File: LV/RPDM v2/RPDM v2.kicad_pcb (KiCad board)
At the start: 2 copper layers, 127.5 x 99.9 mm, 106 parts, among them J2 1-770669-1, J3 776180-1, U1 i7A24045A033V-001-R, U5 OKI-78SR-5_1.5-W36-C

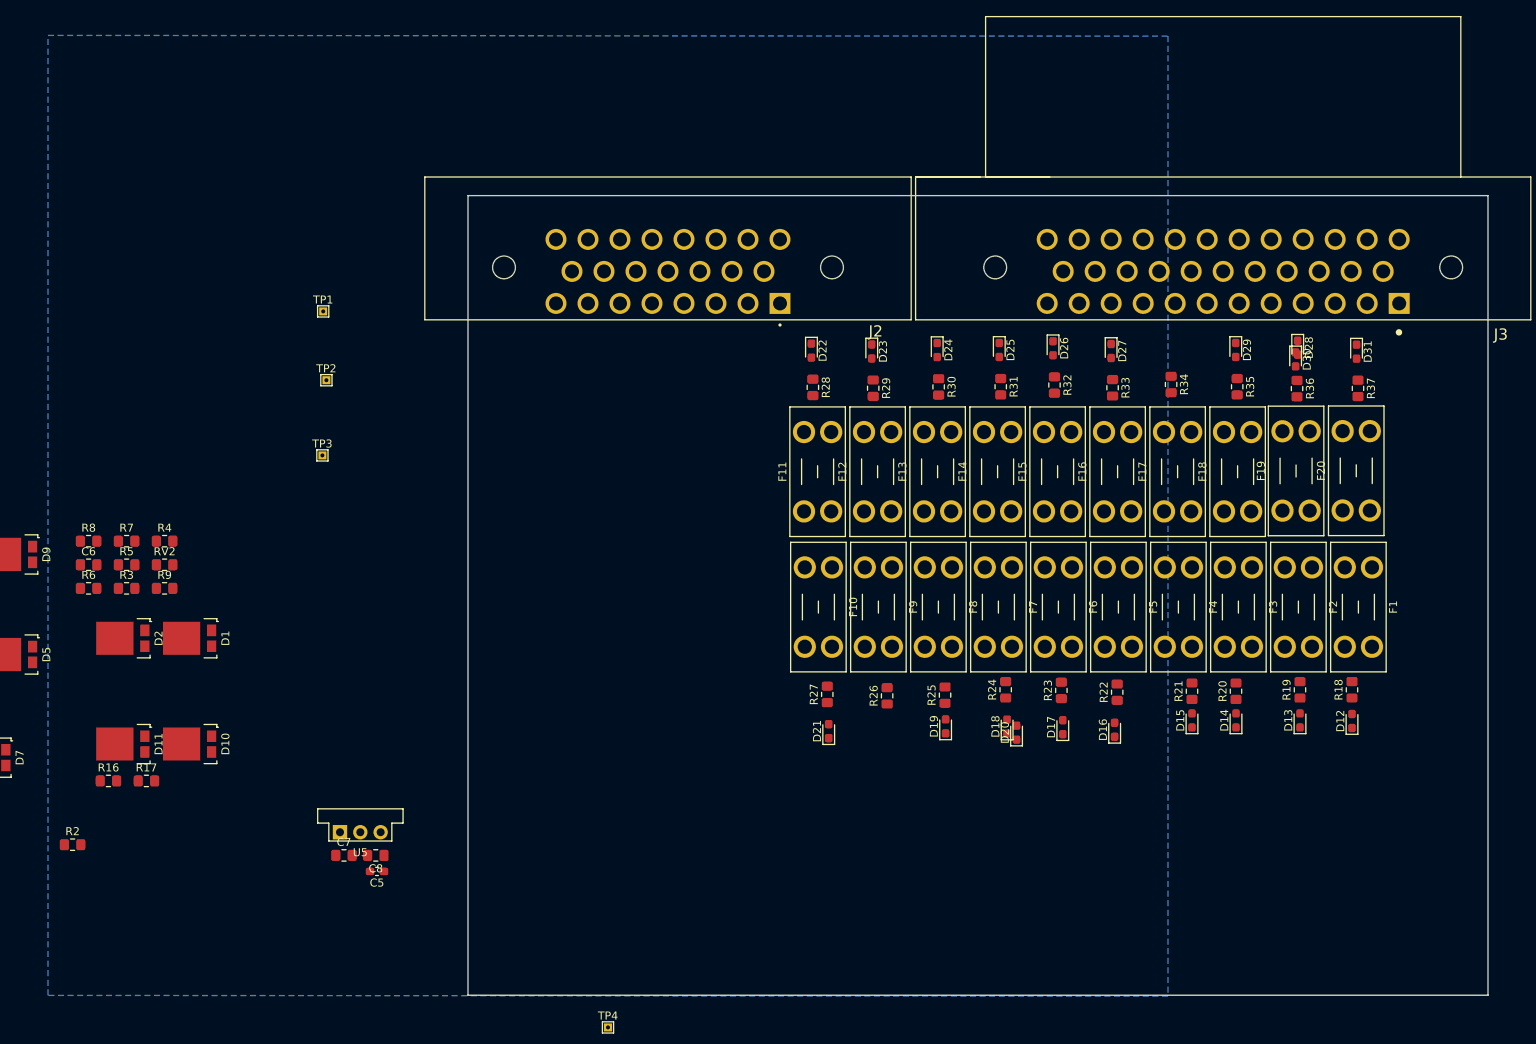
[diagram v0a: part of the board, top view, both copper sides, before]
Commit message: rpdm, libraries cleanup
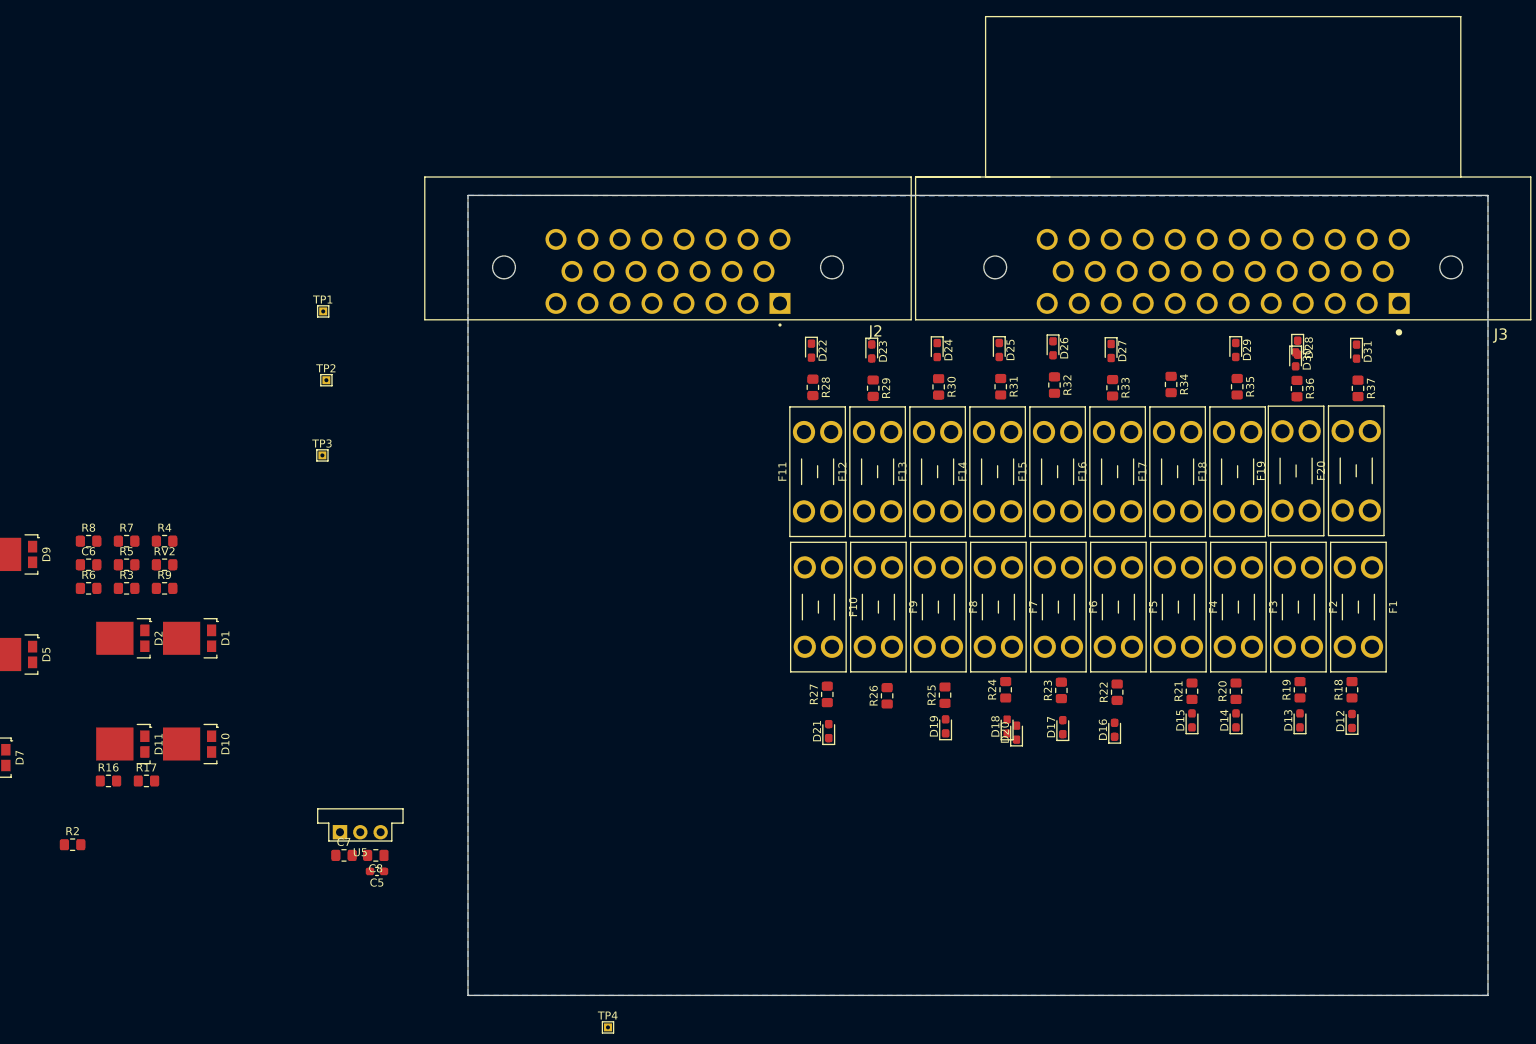
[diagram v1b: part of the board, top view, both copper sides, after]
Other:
- board size 127.5 x 99.9 mm -> 127.5 x 100 mm
- copper layers 2 -> 4
- net class Default: clearance 0.2 -> 0.127; trace_width 0.25 -> 0.127; via_dia 0.8 -> 0.6; via_drill 0.4 -> 0.3
- rule trace_clearance: 0.2 -> 0.127
- rule trace_min: 0.2 -> 0.127
- rule via_min_size: 0.4 -> 0.6

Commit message: RPDM
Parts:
- removed D27, D28, D31: OK_LED, Diode_SMD:D_0603_1608Metric_Pad1.05x0.95mm_HandSolder
- removed F19, F20: Fuse, Fuse:Fuseholder_Blade_Mini_Keystone_3568
- removed R34, R35: 10k, Resistor_SMD:R_0805_2012Metric_Pad1.15x1.40mm_HandSolder
- removed U1: i7A24045A033V-001-R, DCDC:i7A24045A033V
- added C10: 330uF, Capacitor_THT:CP_Radial_D10.0mm_P5.00mm, F.Cu at (303.3, 213.1)
- added C9: 22µF, UOWM_Capacitors:C_Murata_KCM55, F.Cu at (293.7, 212.3)
- added J1: 24V_IN, UOWM_TerminalBlocks:EB167A-03-M, F.Cu at (195.3, 201.1)
- added K1: G8NW, UOWM_Relays:Omron-G8NW-2L-AS_SK-MFG, F.Cu at (301.4, 181.4)
- added K2: G8NW, UOWM_Relays:Omron-G8NW-2L-AS_SK-MFG, F.Cu at (317.7, 181.4)
- added K3: J115F, UOWM_Relays:CIT_J115F1, F.Cu at (237.9, 208.2)
- added Q1: Q_Dual_PMOS, Package_SO:TSOP-6_1.65x3.05mm_P0.95mm, F.Cu at (175.8, 186.3)
- added Q2: Q_Dual_NMOS, UOWM_Package_SO:Diodes_SO-8_5.3x6.2mm_P1.27mm, B.Cu at (309.7, 248.4)
- added Q3: Q_Dual_NMOS, UOWM_Package_SO:Diodes_SO-8_5.3x6.2mm_P1.27mm, F.Cu at (333.4, 250.0)
- added R38: 10k, Resistor_SMD:R_0805_2012Metric_Pad1.15x1.40mm_HandSolder, B.Cu at (160.8, 188.2)
- added U3: OKI-78SR-5_1.5-W36-C, Converter_DCDC:Converter_DCDC_muRata_OKI-78SR_Vertical, F.Cu at (321.0, 213.5)
- added U4: ACS71240, UOWM_Sensors:Allegro_MicroSystems_LLC-LCB-8-0-0-IPC_A, F.Cu at (246.8, 195.2)
- C1: value 330µF -> 0.1µF; footprint Capacitor_THT:CP_Radial_D10.0mm_P5.00mm -> Capacitor_SMD:C_0603_1608Metric_Pad1.05x0.95mm_HandSolder
- C2: value 22µF -> 1uF; footprint Capacitor_extra:C_Murata_KCM55 -> Capacitor_SMD:C_0805_2012Metric_Pad1.15x1.40mm_HandSolder; moved to B.Cu
- C3: value 22µF -> 0.1µF; footprint Capacitor_extra:C_Murata_KCM55 -> Capacitor_SMD:C_0603_1608Metric_Pad1.05x0.95mm_HandSolder; moved to B.Cu
- C4: value 330uF -> 22µF; footprint Capacitor_THT:CP_Radial_D10.0mm_P5.00mm -> Capacitor_SMD:C_0805_2012Metric_Pad1.15x1.40mm_HandSolder; moved to B.Cu
- C5: value 0.1µF -> 22µF; footprint Capacitor_SMD:C_0603_1608Metric_Pad1.05x0.95mm_HandSolder -> Capacitor_SMD:C_0805_2012Metric_Pad1.15x1.40mm_HandSolder; moved to B.Cu
- C6: value 1uF -> 0.1µF; footprint Capacitor_SMD:C_0805_2012Metric_Pad1.15x1.40mm_HandSolder -> Capacitor_SMD:C_0603_1608Metric_Pad1.05x0.95mm_HandSolder; moved to B.Cu
- C7: value 22µF -> 330µF; footprint Capacitor_SMD:C_0805_2012Metric_Pad1.15x1.40mm_HandSolder -> Capacitor_THT:CP_Radial_D10.0mm_P5.00mm
- C8: footprint Capacitor_SMD:C_0805_2012Metric_Pad1.15x1.40mm_HandSolder -> UOWM_Capacitors:C_Murata_KCM55
- D1, D2, D4, D5, D6, D7, D8: footprint Diode_UOWM:TO-277_FSV10150V -> UOWM_Diodes:TO-277_FSV10150V; moved to B.Cu
- D10, D11, D9: value D_Schottky_Flyback -> OK_LED; footprint Diode_UOWM:TO-277_FSV10150V -> Diode_SMD:D_0603_1608Metric_Pad1.05x0.95mm_HandSolder
- D29: value OK_LED -> PWR_ON_LED
- D3: value PWR_ON_LED -> D_Schottky_Flyback; footprint Diode_SMD:D_0603_1608Metric_Pad1.05x0.95mm_HandSolder -> UOWM_Diodes:TO-277_FSV10150V; moved to B.Cu
- D30: value OK_LED -> D_Schottky_Flyback; footprint Diode_SMD:D_0603_1608Metric_Pad1.05x0.95mm_HandSolder -> UOWM_Diodes:TO-277_FSV10150V; moved to B.Cu
- F1, F10, F11, F12, F13, F14, F15, F16, F17, F18, F2, F3, F4, F5, F6, F7, F8, F9: footprint Fuse:Fuseholder_Blade_Mini_Keystone_3568 -> UOWM_Fuses:Keystone_3568
- J2: footprint 1-770669-1:TE_1-770669-1 -> UOWM_Connectors:TE_1-770669-1
- J3: footprint 776180-1:TE_776180-1 -> UOWM_Connectors:TE_1-770669-1
- R1, R2, R8: value 10k -> 100k; moved to B.Cu
- R10, R11, R18, R19, R20, R21, R22, R23, R24, R25, R26, R27, R28, R29, R30, R31, R32, R33, R36: moved to B.Cu
- R16: value 100k -> 10k; moved to B.Cu
- R17: value 470 -> 10k; moved to B.Cu
- R37, R9: value 10k -> 470; moved to B.Cu
- R4, R5: value 100k -> 470
- R6, R7: value 470 -> 10k
- RV1: value 50k -> 100k; footprint Resistor_SMD:R_0805_2012Metric_Pad1.15x1.40mm_HandSolder -> UOWM_Potentiometers:TRIM_3214W
- RV2: value 100k -> 1k; footprint Resistor_SMD:R_0805_2012Metric_Pad1.15x1.40mm_HandSolder -> UOWM_Potentiometers:TRIM_3214W
- U5: value OKI-78SR-5_1.5-W36-C -> i7A24045A033V-001-R; footprint Converter_DCDC:Converter_DCDC_muRata_OKI-78SR_Vertical -> UOWM_DCDCs:i7A24045A033V
- moved R15 336.1 mm to (329.3, 246.8), turned to 90 degrees
- moved R14 333.2 mm to (330.8, 246.8), turned to 270 degrees
- moved R13 331.7 mm to (332.3, 246.8), turned to 90 degrees
- moved R12 328.7 mm to (333.8, 246.8), turned to 270 degrees
- moved R11 316.3 mm to (314.0, 245.3), turned to 90 degrees
- moved R10 310.3 mm to (312.1, 245.3), turned to 270 degrees
- moved R8 302.8 mm to (308.8, 245.4), turned to 270 degrees
- moved D9 299.6 mm to (321.3, 190.3), turned to 180 degrees
- moved D6 299.5 mm to (320.8, 171.2), turned to 180 degrees
- moved D8 294.5 mm to (313.4, 171.2), turned to 180 degrees
- moved D5 294.3 mm to (321.8, 182.8), turned to 180 degrees
- moved R9 292.9 mm to (310.3, 245.4), turned to 90 degrees
- moved D7 286.4 mm to (313.5, 182.8), turned to 180 degrees
- moved R16 280.2 mm to (321.3, 191.6)
- moved D4 275.6 mm to (297.1, 171.3), turned to 180 degrees
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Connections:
- C1 pad 1: /DCDC/24V_IN -> /12V
- C2 pad 1: /DCDC/24V_IN -> Net-(C2-Pad1)
- C3 pad 1: VCC -> /12V
- C4 pad 1: VCC -> /5V_DCDC
- C6 pad 1: Net-(C6-Pad1) -> /5V
- C7 pad 1: /5V_DCDC -> /24_DCDC_IN
- C8 pad 1: /5V -> /24_DCDC_IN
- D1 pad 1: GND -> Net-(D1-Pad1)
- D1 pad 2: GND -> Net-(D1-Pad1)
- D1 pad 3: /+24V_EXT -> /RELAY_3
- D10 pad 1: Net-(D10-Pad1) -> GND
- D10 pad 2: Net-(D10-Pad1) -> Net-(D10-Pad2)
- D11 pad 2: GND -> Net-(D11-Pad2)
- D2 pad 3: /I/V sense/V_IN -> /RAD_FANS
- D3 pad 1: GND -> Net-(D3-Pad1)
- D3 pad 2: Net-(D3-Pad2) -> Net-(D3-Pad1)
- D30 pad 2: Net-(D30-Pad2) -> GND
- D4 pad 1: Net-(D4-Pad1) -> GND
- D4 pad 2: Net-(D4-Pad1) -> GND
- D4 pad 3: /RELAY_3 -> /PUMPS
- D5 pad 1: GND -> Net-(D5-Pad1)
- D5 pad 2: GND -> Net-(D5-Pad1)
- D5 pad 3: /SPARE_RELAY_1 -> /RELAY_1
- D6 pad 1: Net-(D6-Pad1) -> GND
- D6 pad 2: Net-(D6-Pad1) -> GND
- D6 pad 3: /RELAY_4 -> /SPARE_RELAY_1
- D7 pad 1: GND -> Net-(D7-Pad1)
- D7 pad 2: GND -> Net-(D7-Pad1)
- D7 pad 3: /SPARE_RELAY_2 -> /RELAY_2
- D8 pad 1: Net-(D8-Pad1) -> GND
- D8 pad 2: Net-(D8-Pad1) -> GND
- D8 pad 3: /RELAY_1 -> /SPARE_RELAY_2
- D9 pad 2: GND -> Net-(D9-Pad2)
- F1 pad 1: VCC -> /12V
- F1 pad 2: /ACC_FAN_1 -> /RELAY_1
- F10 pad 1: VCC -> /12V
- F10 pad 2: /TSAL -> /MOTOR_CONTROLLER_1
- F11 pad 1: VCC -> /12V
- F11 pad 2: /MOTOR_CONTROLLER_1 -> /MOTOR_CONTROLLER_2
- F12 pad 1: VCC -> /12V
- F12 pad 2: /MOTOR_CONTROLLER_2 -> /ACCUMULATOR
- F13 pad 1: VCC -> /12V
- F13 pad 2: /BRAKE_LIGHT -> /BMS_DATALOGGER
- F14 pad 1: VCC -> /12V
- F14 pad 2: /PDOC_12V -> /HV_DIST
- F15 pad 1: VCC -> /12V
- F15 pad 2: /RELAY_1 -> /INTERLOCK
- F16 pad 1: VCC -> /12V
- F16 pad 2: /RELAY_2 -> /TSAL_PWR
- F17 pad 1: VCC -> /12V
- F17 pad 2: /RELAY_3 -> /BRAKE_LIGHT
- F18 pad 1: VCC -> /12V
- F18 pad 2: /RELAY_4 -> /PDOC_12V
- F2 pad 1: VCC -> /12V
- F2 pad 2: /ACC_FAN_2 -> /RELAY_2
- F3 pad 1: VCC -> /12V
- F3 pad 2: /ACC_FAN_3 -> /RELAY_3
- F4 pad 1: VCC -> /12V
- F4 pad 2: /ACCUMULATOR -> /RELAY_4
- F5 pad 1: VCC -> /12V
- F5 pad 2: /BMS_DATALOGGER -> /SPARE_FUSE_1
- F6 pad 1: VCC -> /12V
- F6 pad 2: /FPDM -> /SPARE_FUSE_2
- F7 pad 1: VCC -> /12V
- F7 pad 2: /HV_DIST -> /ACC_FANS
- F8 pad 1: VCC -> /12V
- F8 pad 2: /INTERLOCK -> /5V_DCDC
- F9 pad 1: VCC -> /12V
- F9 pad 2: /5V_DCDC -> /FPDM
- J2 pad 13: /RAD_FAN_Trigger -> GND
- J2 pad 14: /PUMP_1_Trigger -> GND
- J2 pad 15: /SPARE_Trigger_1 -> GND
- J2 pad 16: /SPARE_Trigger_2 -> /RAD_FAN_Trigger
- J2 pad 17: /TSAT -> /PUMP_1_Trigger
- J2 pad 18: /TSAL_Red -> /SPARE_Trigger_1
- J2 pad 19: /TSAL_Green -> /SPARE_Trigger_2
- J2 pad 20: /BATT_V -> GND
- J2 pad 21: (no net) -> /TSAT
- J2 pad 22: GND -> /TSAL_Red
- J2 pad 23: GND -> /TSAL_Green
- J2 pad 3: /SPARE_FUSE_1 -> /RAD_FANS
- J2 pad 4: /SPARE_FUSE_2 -> /PUMPS
- J2 pad 5: (no net) -> /SPARE_FUSE_1
- J2 pad 6: GND -> /SPARE_FUSE_2
- J2 pad 7: GND -> /ACC_FANS
- J2 pad 8: GND -> /ACC_FANS
- J3 pad 1: /ACC_FAN_1 -> /FPDM
- J3 pad 10: /MOTOR_CONTROLLER_2 -> GND
- J3 pad 11: /5V -> GND
- J3 pad 12: /TSAL -> GND
- J3 pad 13: /BRAKE_LIGHT -> GND
- J3 pad 14: /PDOC_12V -> GND
- J3 pad 15: /RAD_FANS -> GND
- J3 pad 16: /RAD_FANS -> /5V
- J3 pad 17: /PUMPS -> /BATT_V
- J3 pad 18: /PUMPS -> /BATT_I
- J3 pad 2: /ACC_FAN_2 -> /MOTOR_CONTROLLER_1
- J3 pad 22: GND -> /PDOC_12V
- J3 pad 23: GND -> /BRAKE_LIGHT
- J3 pad 3: /ACC_FAN_3 -> /MOTOR_CONTROLLER_2
- J3 pad 6: /FPDM -> /HV_DIST
- J3 pad 7: /HV_DIST -> /INTERLOCK
- J3 pad 8: /INTERLOCK -> /TSAL_PWR
- J3 pad 9: /MOTOR_CONTROLLER_1 -> GND
- R1 pad 1: VCC -> (no net)
- R1 pad 2: Net-(D3-Pad2) -> Net-(R1-Pad2)
- R10 pad 1: /SPARE_Trigger_1 -> /PUMP_1_Trigger
- R11 pad 1: (no net) -> Net-(Q2-Pad4)
- R11 pad 2: /SPARE_Trigger_1 -> /PUMP_1_Trigger
- R12 pad 1: /SPARE_Trigger_2 -> /SPARE_Trigger_1
- R13 pad 1: (no net) -> Net-(Q3-Pad2)
- R13 pad 2: /SPARE_Trigger_2 -> /SPARE_Trigger_1
- R14 pad 1: /RAD_FAN_Trigger -> /SPARE_Trigger_2
- R15 pad 1: (no net) -> Net-(Q3-Pad4)
- R15 pad 2: /RAD_FAN_Trigger -> /SPARE_Trigger_2
- R16 pad 1: /PUMP_1_Trigger -> Net-(D9-Pad2)
- R16 pad 2: GND -> /RELAY_1
- R17 pad 1: (no net) -> Net-(D10-Pad2)
- R17 pad 2: /PUMP_1_Trigger -> /RELAY_2
- R18 pad 1: Net-(D12-Pad2) -> Net-(D11-Pad2)
- R18 pad 2: /ACC_FAN_1 -> /RELAY_3
- R19 pad 1: Net-(D13-Pad2) -> Net-(D12-Pad2)
- R19 pad 2: /ACC_FAN_2 -> /RELAY_4
- R2 pad 1: /I/V sense/V_IN -> /alt TSAL Logic/NAND_Out
- R2 pad 2: /BATT_V -> /12V
- R20 pad 1: Net-(D14-Pad2) -> Net-(D13-Pad2)
- R20 pad 2: /ACC_FAN_3 -> /SPARE_FUSE_1
- R21 pad 1: Net-(D15-Pad2) -> Net-(D14-Pad2)
- R21 pad 2: /ACCUMULATOR -> /SPARE_FUSE_2
- R22 pad 1: Net-(D16-Pad2) -> Net-(D15-Pad2)
- R22 pad 2: /BMS_DATALOGGER -> /ACC_FANS
- R23 pad 1: Net-(D17-Pad2) -> Net-(D16-Pad2)
- R23 pad 2: /FPDM -> /5V_DCDC
- R24 pad 1: Net-(D18-Pad2) -> Net-(D17-Pad2)
- R24 pad 2: /HV_DIST -> /MOTOR_CONTROLLER_2
- R25 pad 1: Net-(D19-Pad2) -> Net-(D18-Pad2)
- R25 pad 2: /INTERLOCK -> /ACCUMULATOR
- R26 pad 1: Net-(D20-Pad2) -> Net-(D19-Pad2)
- R26 pad 2: /5V_DCDC -> /FPDM
- R27 pad 1: Net-(D21-Pad2) -> Net-(D20-Pad2)
- R27 pad 2: /TSAL -> /MOTOR_CONTROLLER_1
- R28 pad 1: Net-(D22-Pad2) -> Net-(D21-Pad2)
- R28 pad 2: /MOTOR_CONTROLLER_1 -> /BMS_DATALOGGER
- R29 pad 1: Net-(D23-Pad2) -> Net-(D22-Pad2)
- R29 pad 2: /MOTOR_CONTROLLER_2 -> /HV_DIST
- R3 pad 1: VCC -> GND
- R3 pad 2: Net-(R3-Pad2) -> /TSAT
- R30 pad 1: Net-(D24-Pad2) -> Net-(D23-Pad2)
- R30 pad 2: /BRAKE_LIGHT -> /INTERLOCK
- R31 pad 1: Net-(D25-Pad2) -> Net-(D24-Pad2)
- R31 pad 2: /PDOC_12V -> /TSAL_PWR
- R32 pad 1: Net-(D26-Pad2) -> Net-(D25-Pad2)
- R32 pad 2: /RELAY_1 -> /BRAKE_LIGHT
- R33 pad 1: Net-(D27-Pad2) -> Net-(D26-Pad2)
- R33 pad 2: /RELAY_2 -> /PDOC_12V
- R36 pad 1: Net-(D30-Pad2) -> /24_ISENSE_IN
- R36 pad 2: /SPARE_FUSE_1 -> /BATT_V
- R37 pad 1: Net-(D31-Pad2) -> Net-(R37-Pad1)
- R37 pad 2: /SPARE_FUSE_2 -> Net-(R37-Pad2)
- R4 pad 1: GND -> Net-(Q1-Pad1)
- R5 pad 1: GND -> Net-(Q1-Pad3)
- R6 pad 1: (no net) -> /TSAL_Red
- R6 pad 2: /alt TSAL Logic/NAND_Out -> Net-(Q1-Pad6)
- R7 pad 1: (no net) -> /TSAL_Green
- R7 pad 2: /TSAT -> Net-(Q1-Pad4)
- R8 pad 1: /TSAL_Red -> /RAD_FAN_Trigger
- R8 pad 2: (no net) -> GND
- R9 pad 1: /TSAL_Green -> Net-(Q2-Pad2)
- R9 pad 2: (no net) -> /RAD_FAN_Trigger
- RV1 pad 1: GND -> Net-(C2-Pad1)
- RV1 pad 2: Net-(RV1-Pad2) -> Net-(R1-Pad2)
- RV2 pad 1: Net-(C6-Pad1) -> GND
- RV2 pad 2: Net-(R3-Pad2) -> Net-(R37-Pad2)
- TP3 pad 1: (no net) -> /+24V_BATT
- TP4 pad 1: VCC -> /12V
- U5 pad 1: /5V_DCDC -> /24_DCDC_IN
- U5 pad 3: /5V -> GND
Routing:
- net /12V: track 0.00 -> 61.3 mm
- net /ACC_FANS: track 0.00 -> 30.1 mm
- net /SPARE_FUSE_1: track 0.00 -> 20.5 mm
- net /SPARE_FUSE_2: track 0.00 -> 18.0 mm
- net /SPARE_RELAY_1: track 0.00 -> 16.1 mm
- net /SPARE_RELAY_2: track 0.00 -> 11.6 mm
- net /RAD_FANS: track 0.00 -> 8.52 mm
- net /5V_DCDC: track 0.00 -> 8.49 mm
- net /PUMPS: track 0.00 -> 7.21 mm
- net /FPDM: track 0.00 -> 6.90 mm
- net /INTERLOCK: track 0.00 -> 6.79 mm
- net /PDOC_12V: track 0.00 -> 6.78 mm
- net /TSAL_PWR: track 0.00 -> 6.78 mm
- net /BRAKE_LIGHT: track 0.00 -> 6.78 mm
- net /MOTOR_CONTROLLER_2: track 0.00 -> 6.76 mm
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- added copper zone on B.Cu, net /5V
- added copper zone on B.Cu, net /5V_DCDC
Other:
- board size 127.5 x 100 mm -> 140 x 73 mm
- copper layers 4 -> 2
- net class 12V10A added: clearance 0.2, trace_width 3, via_dia 0.6, via_drill 0.3
- net class 24V2A added: clearance 0.25, trace_width 0.2, via_dia 0.6, via_drill 0.3
- net class 24V31A added: clearance 0.25, trace_width 12.75, via_dia 0.6, via_drill 0.3
- net class Default: clearance 0.127 -> 0.2; trace_width 0.127 -> 0.2
- rule pad_to_mask_clearance: 0 -> 0.05
- rule solder_mask_min_width: 0.12 -> 0.254
- rule trace_clearance: 0.127 -> 0.2
- rule trace_min: 0.127 -> 0.2
- rule via_min_drill: 0.3 -> 0.2
- rule via_min_size: 0.6 -> 0.4

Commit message: RPDM nearly finished
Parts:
- added U1: BU4S584G2, UOWM_Package_SO:SSOP-5_ROHM, B.Cu at (153.8, 88.2)
- added U2: BU4S11G2, UOWM_Package_SO:SSOP-5_ROHM, B.Cu at (153.8, 82.6)
- C3, D2, D4, D6, D8: moved to F.Cu
- C8, C9, Q1, Q3, R12, R13, R14, R15, R3, R4, R5, R6, R7: moved to B.Cu
- moved C1 220.8 mm to (154.7, 86.1), turned to 180 degrees
- moved R4 211.4 mm to (157.2, 78.8), turned to 180 degrees
- moved R12 206.6 mm to (215.2, 77.6), turned to 90 degrees
- moved R2 205.6 mm to (157.9, 81.8), turned to 270 degrees
- moved R14 203.7 mm to (217.3, 77.6), turned to 90 degrees
- moved R13 202.7 mm to (215.2, 81.4)
- moved C3 200.3 mm to (154.7, 80.7), turned to 180 degrees
- moved R15 199.8 mm to (217.3, 81.4)
- moved Q3 198.7 mm to (213.2, 91.8), turned to 0 degrees
- moved R10 194.7 mm to (213.2, 77.6), turned to 90 degrees
- moved R8 194.1 mm to (211.2, 77.6), turned to 90 degrees
- moved R1 193.1 mm to (156.1, 90.0), turned to 180 degrees
- moved C2 192.8 mm to (152.1, 87.0), turned to 90 degrees
- moved R11 192.4 mm to (213.2, 81.4)
- moved R9 191.6 mm to (211.2, 81.4)
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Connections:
- net /12V renamed VCC
- J1 pad 1: /+24V_BATT -> GND
- J1 pad 2: /+24V_EXT -> /+24V_BATT
- J1 pad 3: GND -> /+24V_EXT
- R1 pad 1: (no net) -> Net-(R1-Pad1)
- R4 pad 1: Net-(Q1-Pad1) -> Net-(Q1-Pad3)
- R5 pad 1: Net-(Q1-Pad3) -> Net-(Q1-Pad1)
- R6 pad 2: Net-(Q1-Pad6) -> Net-(Q1-Pad4)
- R7 pad 2: Net-(Q1-Pad4) -> Net-(Q1-Pad6)
- TP2 pad 1: /+24V_EXT -> /+24V_BATT
- TP3 pad 1: /+24V_BATT -> /+24V_EXT
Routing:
- net /5V: track 1.52 -> 132.4 mm, vias 2 -> 6
- net VCC: track 61.3 -> 160.3 mm, vias 0 -> 3
- net /BATT_I: track 0.00 -> 57.8 mm, vias 0 -> 6
- net /24_ISENSE_IN: track 0.00 -> 38.8 mm, vias 0 -> 7
- net GND: track 1.82 -> 40.6 mm, vias 2 -> 31
- net /TSAT: track 0.00 -> 36.5 mm, vias 0 -> 1
- net Net-(D3-Pad1): track 0.00 -> 35.6 mm
- net /PDOC_12V: track 6.78 -> 40.6 mm
- net /FPDM: track 6.90 -> 38.4 mm
- net /SPARE_Trigger_2: track 0.00 -> 31.0 mm, vias 0 -> 1
- net /MOTOR_CONTROLLER_1: track 6.76 -> 35.2 mm
- net /MOTOR_CONTROLLER_2: track 6.76 -> 33.2 mm
- net /SPARE_Trigger_1: track 0.00 -> 24.0 mm, vias 0 -> 1
- net Net-(D7-Pad1): track 0.00 -> 22.9 mm
- net Net-(D1-Pad1): track 0.00 -> 22.6 mm
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- added copper zone on F.Cu, net /+24V_BATT
- added copper zone on B.Cu, net /+24V_EXT
- added copper zone on F.Cu, net /+24V_EXT
- added copper zone on B.Cu, net /24_DCDC_IN
- added copper zone on F.Cu, net /24_DCDC_IN
- added copper zone on F.Cu, net /24_ISENSE_IN
- added copper zone on F.Cu, net /PUMPS
- added copper zone on F.Cu, net /RAD_FANS
- added copper zone on B.Cu, net /RELAY_1
- added copper zone on B.Cu, net /RELAY_2
- added copper zone on B.Cu, net /RELAY_3
- added copper zone on B.Cu, net /RELAY_4
- added copper zone on F.Cu, net /SPARE_FUSE_2
- added copper zone on F.Cu, net /SPARE_RELAY_1
- added copper zone on F.Cu, net /SPARE_RELAY_2
- added copper zone on B.Cu, net VCC
- added copper zone on F.Cu, net VCC
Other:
- board size 140 x 73 mm -> 130 x 75 mm
- rule via_min_size: 0.4 -> 0.6
- board text added: "10A"
- board text added: "2A"
- board text added: "5A"

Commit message: RPDM
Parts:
- added REF**: MountingHole_3.2mm_M3_Pad, MountingHole:MountingHole_3.2mm_M3_Pad, F.Cu at (193.2, 137.1)
- added REF**: MountingHole_3.2mm_M3_Pad, MountingHole:MountingHole_3.2mm_M3_Pad, F.Cu at (117.6, 137.1)
- moved TP4 25.2 mm to (177.3, 119.9)
- moved C4 21.3 mm to (194.4, 124.9), turned to 180 degrees
- moved U3 19.0 mm to (195.7, 126.9), turned to 180 degrees
- moved C5 15.4 mm to (191.9, 128.9), turned to 0 degrees
- moved R36 14.1 mm to (120.3, 68.6)
- moved C10 14.1 mm to (181.8, 126.1)
- moved C2 14.1 mm to (142.1, 77.1)
- moved C3 14.1 mm to (144.7, 70.8)
- moved C7 14.1 mm to (136.2, 118.5)
- moved D1 14.1 mm to (188.5, 98.6)
- moved D10 14.1 mm to (195.5, 105.5)
- moved D11 14.1 mm to (188.1, 105.5)
- moved D12 14.1 mm to (180.7, 105.5)
- moved D17 14.1 mm to (132.7, 83.8)
- moved D19 14.1 mm to (147.7, 83.8)
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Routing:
- net /5V: track 132.4 -> 139.9 mm, vias 6 -> 8
- net /5V_DCDC: track 17.7 -> 21.6 mm
- added copper zone on F.Cu, net /RELAY_1
- added copper zone on F.Cu, net /RELAY_2
- added copper zone on F.Cu, net /RELAY_3
- added copper zone on F.Cu, net /RELAY_4
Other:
- rule via_min_drill: 0.2 -> 0.3

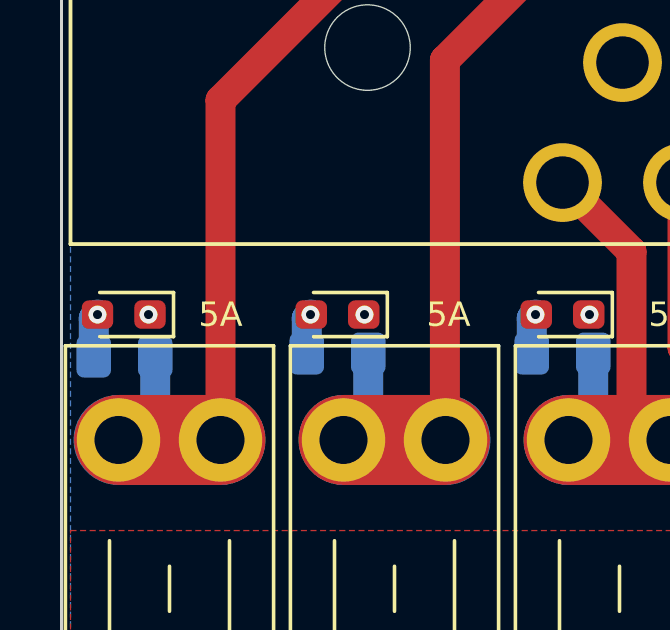
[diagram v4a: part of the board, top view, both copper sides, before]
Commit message: started LV Harness
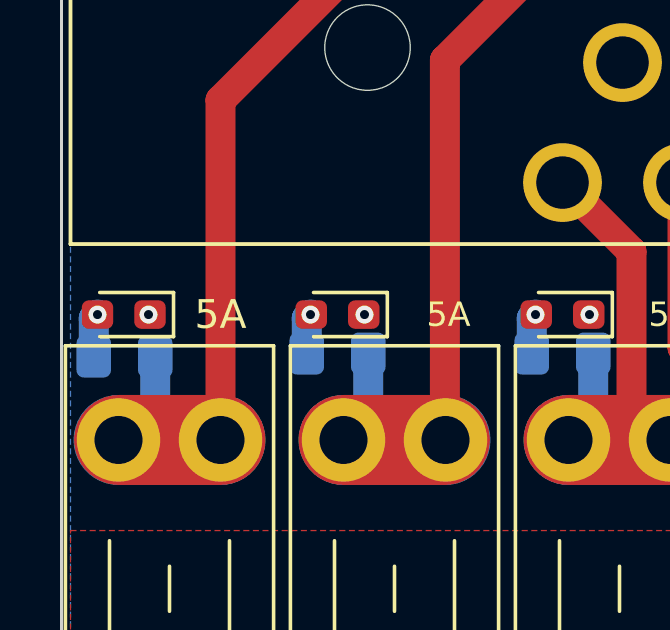
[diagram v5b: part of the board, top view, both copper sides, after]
